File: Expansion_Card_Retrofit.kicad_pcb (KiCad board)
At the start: 8 copper layers, 24 x 27.3 mm, 205 parts, among them J4 Conn_02x02_Odd_Even, P1 1054440011, Q1 CSD25480F3, SW1 KXT 331 LHS, SW2 KXT 331 LHS, U1 TXS0202YZPR, U10 TMP110D, U11 MMC5633NJL, U12 STM32L422RBI6, U2 CCGM1A1, U4 W25Q16JLUXIG TR, U5 USB3740B-AI2, U6 TPS7A2033PDQNR, U7 TPSM82822SILR, U8 TPSM82822SILR, U9 ISM330DHCX, Y1 S3A2505-100.000-L-X1-R

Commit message: RevA
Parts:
- added D7: 16-213SDRC/S530-A3/TR8, LED_SMD:LED_0402_1005Metric, B.Cu at (147.5, 130.2)
- added R20: 60R4, Resistor_SMD:R_0201_0603Metric, B.Cu at (145.8, 130.1)
- moved C2 0.37 mm to (149.8, 133.6)
- moved R1 0.19 mm to (144.7, 154.1), turned to 0 degrees
- moved C4 0.07 mm to (148.8, 133.3)
- moved TP2 0.06 mm to (148.1, 135.0)
- turned D2 to 180 degrees
- turned D3 to 180 degrees
- turned R3 to 180 degrees
- renumbered C125 to C1, C78 to C10, C15 to C100, C14 to C101, C85 to C102, C83 to C103, C84 to C104, C87 to C105, C86 to C106, C88 to C107, C79 to C11, C80 to C12, C46 to C13, C47 to C14, C119 to C15, C1 to C16, C2 to C17, C3 to C18, C65 to C19, C48 to C2, C66 to C20, C67 to C21, C68 to C22, C69 to C23, C70 to C24, C71 to C25, C72 to C26, C73 to C27, C74 to C28, C81 to C29, C49 to C3, C118 to C30, C40 to C31, C39 to C32, C38 to C33, C37 to C34, C36 to C35, C18 to C36, C17 to C37, C16 to C38, C19 to C39, C50 to C4, C20 to C40, C25 to C41, C24 to C42, C23 to C43, C22 to C44, C21 to C45, C26 to C46, C27 to C47, C28 to C48, C29 to C49, C51 to C5, C30 to C50, C31 to C51, C32 to C52, C33 to C53, C34 to C54, C35 to C55, C45 to C56, C44 to C57, C43 to C58, C42 to C59, C54 to C6, C41 to C60, C9 to C61, C10 to C62, C89 to C64, C90 to C65, C64 to C66, C82 to C67, C99 to C68, C100 to C69, C75 to C7, C101 to C70, C102 to C71, C103 to C72, C104 to C73, C105 to C74, C106 to C75, C107 to C76, C108 to C77, C109 to C78, C110 to C79, C76 to C8, C11 to C80, C12 to C81, C13 to C82, C53 to C83, C91 to C84, C92 to C85, C93 to C86, C94 to C87, C95 to C88, C96 to C89, C77 to C9, C97 to C90, C98 to C91, C111 to C92, C112 to C93, C113 to C94, C114 to C95, C115 to C96, C116 to C97, C117 to C98, C52 to C99, D17 to D1, D3 to D10, D4 to D11, D5 to D12, D6 to D13, D10 to D2, D11 to D3, D16 to D4, D15 to D5, D9 to D6, D1 to D8, D2 to D9, FID5 to FID3, FID3 to FID4, FID4 to FID5, J4 to J1, R13 to R1, R23 to R10, R38 to R11, R39 to R12, R52 to R13, R2 to R14, R48 to R15, R49 to R16, R21 to R17, R29 to R18, R30 to R19, R47 to R2, R26 to R21, R27 to R22, R5 to R23, R19 to R24, R20 to R25, R6 to R26, R28 to R27, R7 to R28, R25 to R29, R14 to R3, R43 to R30, R44 to R31, R8 to R32, R32 to R34, R36 to R35, R17 to R36, R46 to R38, R41 to R39, R50 to R4, R42 to R40, R51 to R41, R15 to R42, R31 to R43, R4 to R44, R16 to R45, R22 to R46, R53 to R47, R9 to R48, R11 to R49, R34 to R5, R10 to R50, R24 to R51, R40 to R52, R35 to R53, R3 to R6, R18 to R7, R12 to R8, R45 to R9, TP7 to TP1, TP8 to TP2, TP5 to TP3, TP6 to TP4, TP1 to TP5, TP2 to TP6, TP3 to TP7, TP4 to TP8, U5 to U1, U7 to U10, U8 to U11, U4 to U2, U2 to U3, U12 to U4, U1 to U5, U11 to U6, U10 to U7, U9 to U8, U6 to U9
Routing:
- net GND: track 109.3 -> 104.3 mm, vias 133 -> 135
- net +2V5: track 64.5 -> 66.0 mm, vias 79 -> 82
- net /RX2_P: track 23.4 -> 22.3 mm
- net /~{FPGA_RST}: track 36.8 -> 37.8 mm
- net Net-(D7-K): track 0.00 -> 0.94 mm
- net /TX0: track 29.5 -> 28.7 mm
- net /~{FLASH_CS}: track 27.8 -> 28.5 mm
- net /RX2_N: track 23.5 -> 22.9 mm
- net /BOOT0: track 32.8 -> 33.3 mm
- net /VBUS_UNPROTECTED: vias 4 -> 3
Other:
- board text added: "0.075 mm"
- board text added: "0.0764 mm"
- board text added: "0.0900 mm / 0.0889 mm"
- board text added: "0.2000 mm"
- board text added: "0.8844 mm"
- board text added: "8"
- board text added: "ENIG"
- board text added: "SWK"
- board text added: "Yes"
- board text removed: "0.025 mm"
- board text removed: "0.04 mm"
- board text removed: "0.1 mm"
- board text removed: "0.2 mm"
- board text removed: "SWCLK"

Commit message: add readme
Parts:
- U7: value TMP110D -> TMP110D1IDPWR

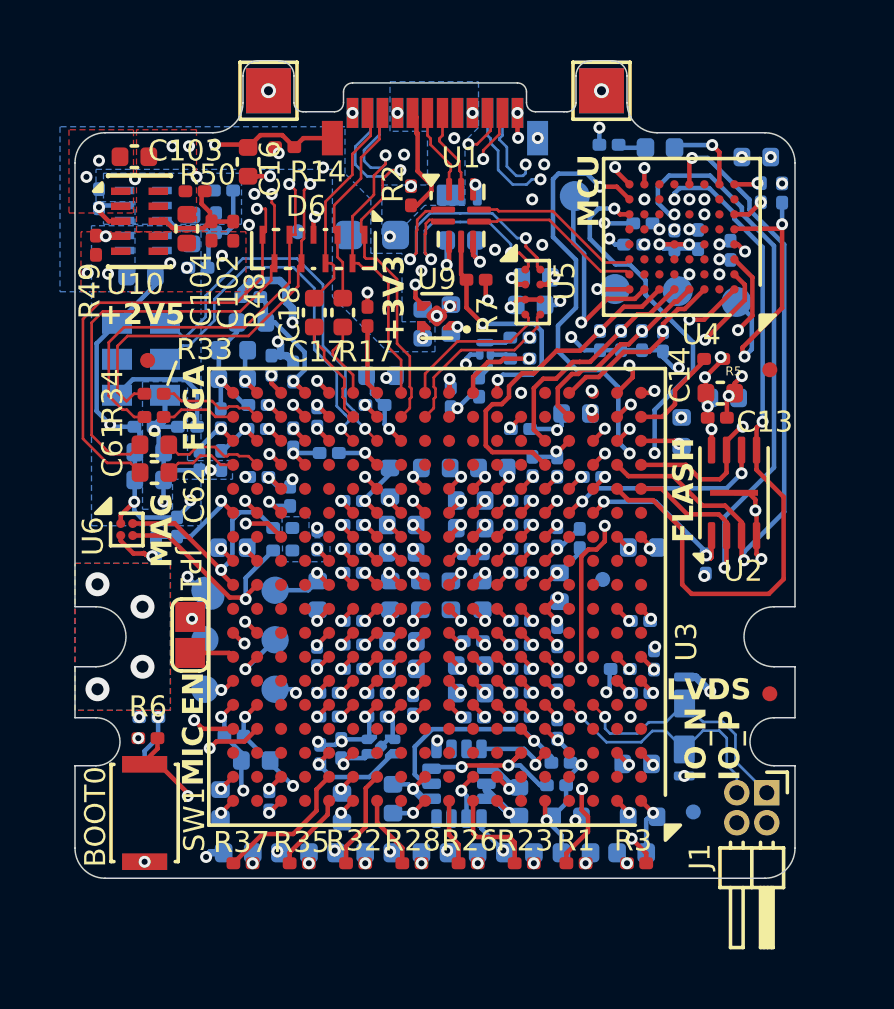
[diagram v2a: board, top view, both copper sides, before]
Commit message: fix a clearance issue
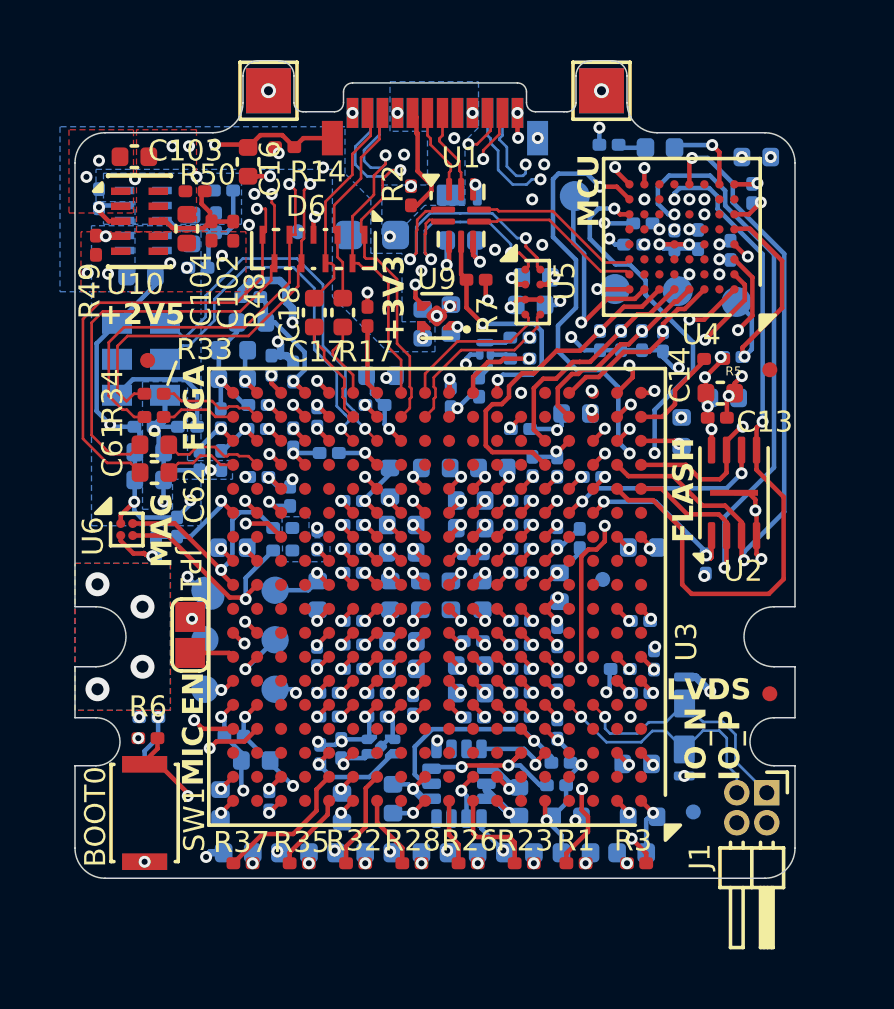
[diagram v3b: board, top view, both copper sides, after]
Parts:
- moved R4 5.71 mm to (149.9, 137.2), turned to 0 degrees
- moved C5 0.29 mm to (150.6, 131.7)
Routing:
- net /~{RST}: track 9.58 -> 7.94 mm, vias 2 -> 1
- net +2V5: vias 82 -> 81
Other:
- board text removed: "0.1524 mm / 0.0000 mm"
- board text removed: "0.3000 mm"
- board text removed: "0.8000 mm"
- board text removed: "2"
- board text removed: "None"
